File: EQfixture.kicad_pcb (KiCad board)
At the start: 2 copper layers, 149.8 x 111.4 mm, 14 parts, among them J1 Screw_Terminal_01x02, J2 Screw_Terminal_01x02, J3 Screw_Terminal_01x02, J4 Conn_02x10_Top_Bottom, J5 Screw_Terminal_01x03, J6 Conn_01x03, J7 Conn_01x06_Female

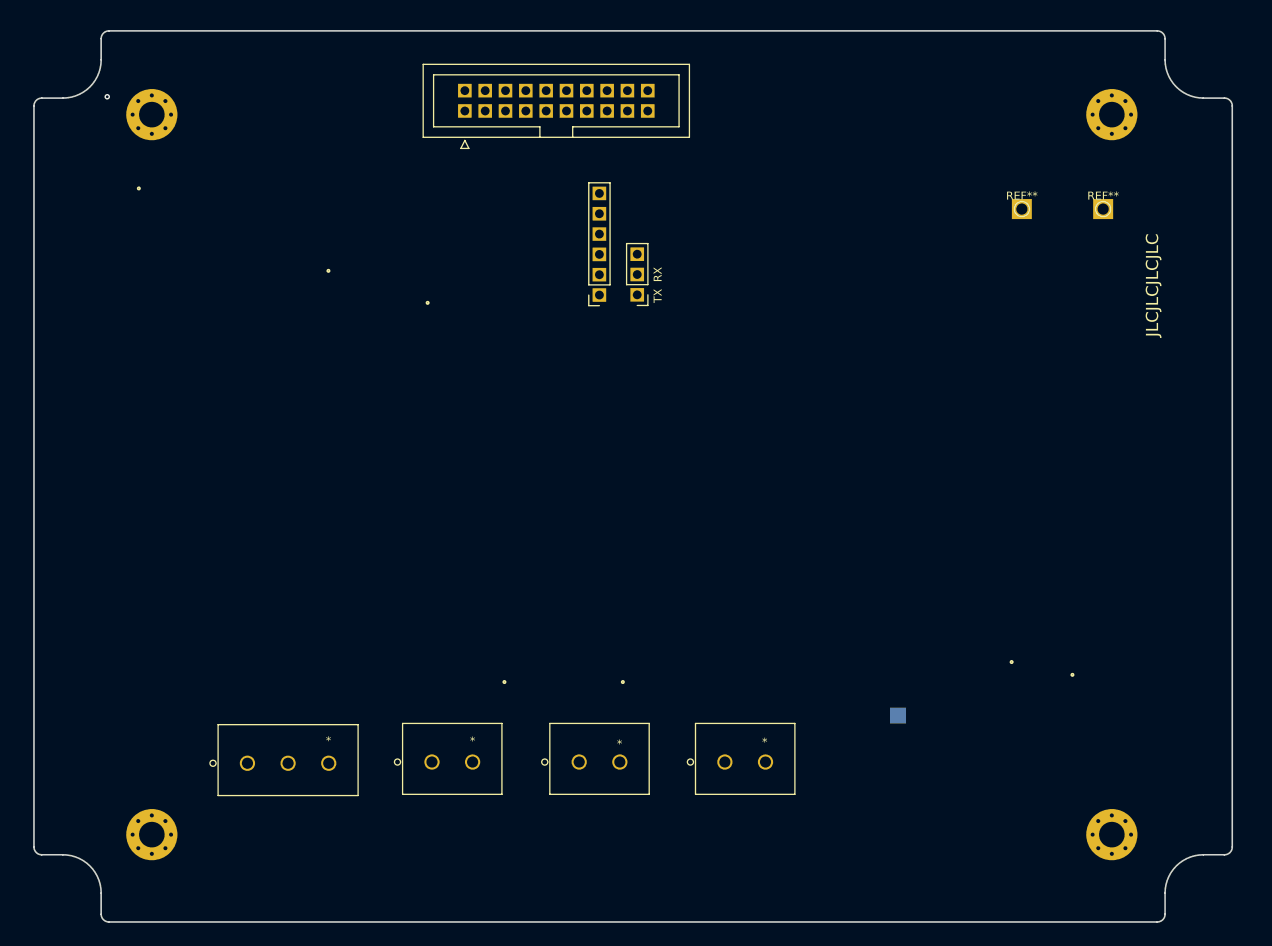
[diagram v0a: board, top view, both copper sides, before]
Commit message: pogos added
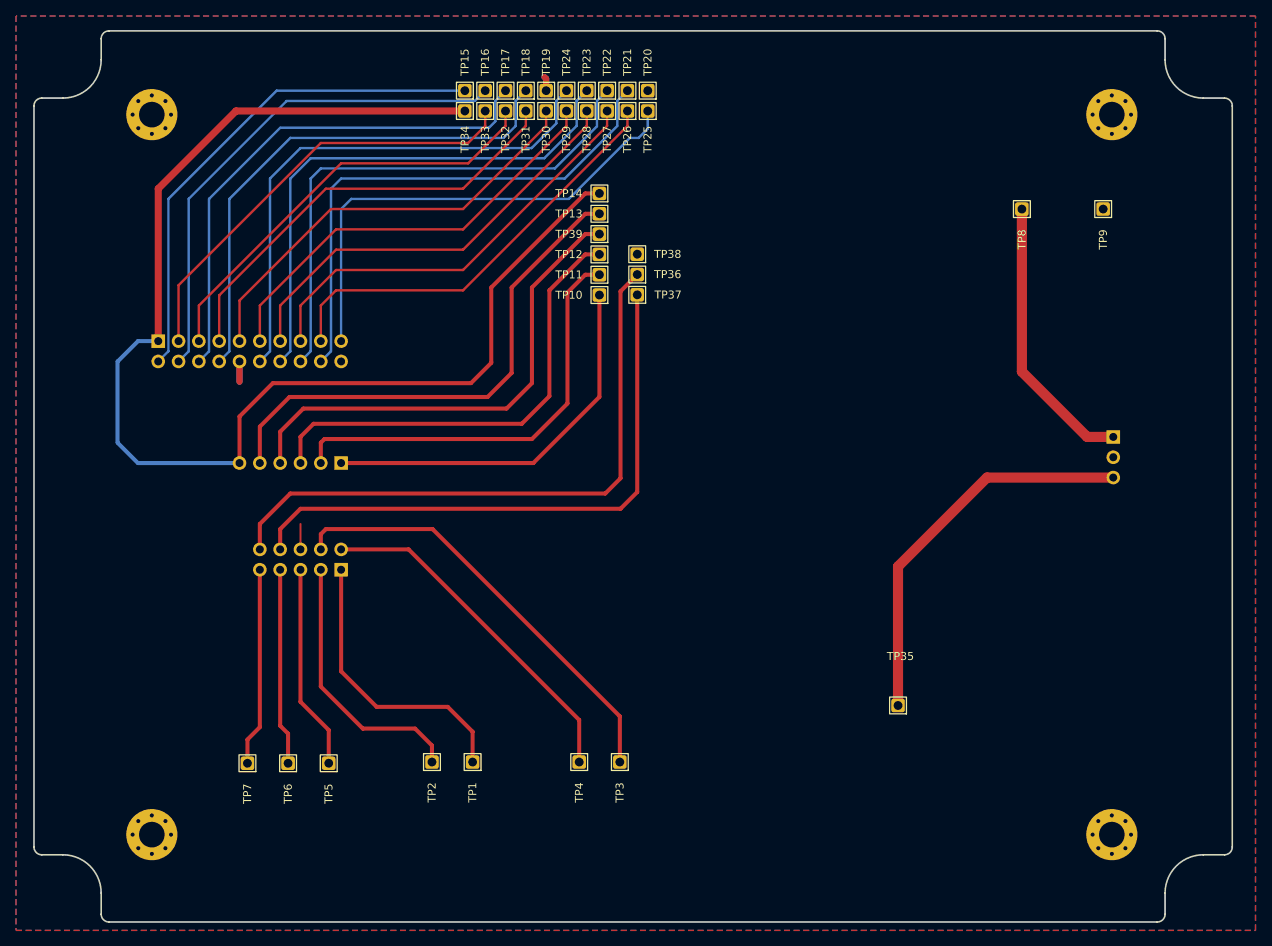
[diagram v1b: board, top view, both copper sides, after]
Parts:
- removed J5: Screw_Terminal_01x03, NLC:Phoenix_3P_1755749
- removed J6: Conn_01x03, Connector_PinHeader_2.54mm:PinHeader_1x03_P2.54mm_Vertical
- removed J7: Conn_01x06_Female, Connector_PinSocket_2.54mm:PinSocket_1x06_P2.54mm_Vertical
- removed REF** (x2): TestPoint_THTPad_D1.5mm_Drill0.7mm, TestPoint:TestPoint_THTPad_D1.5mm_Drill0.7mm
- added TP10: SWO, my_footprints:TestPoint-TH-Square-1mmHole, F.Cu at (145.5, 67.6)
- added TP11: NRST, my_footprints:TestPoint-TH-Square-1mmHole, F.Cu at (145.5, 65.1)
- added TP12: GND, my_footprints:TestPoint-TH-Square-1mmHole, F.Cu at (145.5, 62.5)
- added TP13: SWCLK, my_footprints:TestPoint-TH-Square-1mmHole, F.Cu at (145.5, 57.4)
- added TP14: 3V3, my_footprints:TestPoint-TH-Square-1mmHole, F.Cu at (145.5, 54.9)
- added TP15: I2C_SDA, my_footprints:TestPoint-TH-Square-1mmHole, F.Cu at (128.7, 42.1)
- added TP16: ~{LED_BAT_OK}, my_footprints:TestPoint-TH-Square-1mmHole, F.Cu at (131.2, 42.1)
- added TP17: ~{LED_FAIL}, my_footprints:TestPoint-TH-Square-1mmHole, F.Cu at (133.7, 42.1)
- added TP18: ~{LED_TRIGGER}, my_footprints:TestPoint-TH-Square-1mmHole, F.Cu at (136.3, 42.1)
- added TP19: GND, my_footprints:TestPoint-TH-Square-1mmHole, F.Cu at (138.8, 42.1)
- added TP2: R_TST_G, my_footprints:TestPoint-TH-Square-1mmHole, F.Cu at (124.5, 126.0)
- added TP20: GND, my_footprints:TestPoint-TH-Square-1mmHole, F.Cu at (151.5, 42.1)
- added TP21: LED_BAT_DONE, my_footprints:TestPoint-TH-Square-1mmHole, F.Cu at (149.0, 42.1)
- added TP22: SW_UP, my_footprints:TestPoint-TH-Square-1mmHole, F.Cu at (146.4, 42.1)
- added TP23: SW_TST_EVENT, my_footprints:TestPoint-TH-Square-1mmHole, F.Cu at (143.9, 42.1)
- added TP24: SW_RST_EVENT, my_footprints:TestPoint-TH-Square-1mmHole, F.Cu at (141.4, 42.1)
- added TP25: LED_BAT_CHRG, my_footprints:TestPoint-TH-Square-1mmHole, F.Cu at (151.5, 44.6)
- added TP26: SW_DOWN, my_footprints:TestPoint-TH-Square-1mmHole, F.Cu at (149.0, 44.6)
- added TP27: SW_ENTER, my_footprints:TestPoint-TH-Square-1mmHole, F.Cu at (146.4, 44.6)
- added TP28: SW_EXIT, my_footprints:TestPoint-TH-Square-1mmHole, F.Cu at (143.9, 44.6)
- added TP29: LED_RUNNING, my_footprints:TestPoint-TH-Square-1mmHole, F.Cu at (141.4, 44.6)
- added TP3: R_RST, my_footprints:TestPoint-TH-Square-1mmHole, F.Cu at (148.0, 126.0)
- added TP30: LED_TRIGGER, my_footprints:TestPoint-TH-Square-1mmHole, F.Cu at (138.8, 44.6)
- added TP31: LED_FAIL, my_footprints:TestPoint-TH-Square-1mmHole, F.Cu at (136.3, 44.6)
- added TP32: LED_STANDBY, my_footprints:TestPoint-TH-Square-1mmHole, F.Cu at (133.7, 44.6)
- added TP33: I2C_SCL, my_footprints:TestPoint-TH-Square-1mmHole, F.Cu at (131.2, 44.6)
- added TP34: 3V3, my_footprints:TestPoint-TH-Square-1mmHole, F.Cu at (128.7, 44.6)
- added TP35: VCC_BATT, my_footprints:TestPoint-TH-Square-1mmHole, F.Cu at (182.8, 118.9)
- added TP36: RX, my_footprints:TestPoint-TH-Square-1mmHole, F.Cu at (150.2, 65.0)
- added TP37: TX, my_footprints:TestPoint-TH-Square-1mmHole, F.Cu at (150.2, 67.6)
- added TP38: GND, my_footprints:TestPoint-TH-Square-1mmHole, F.Cu at (150.2, 62.5)
- added TP39: SWDIO, my_footprints:TestPoint-TH-Square-1mmHole, F.Cu at (145.5, 60.0)
- added TP4: R_RST_G, my_footprints:TestPoint-TH-Square-1mmHole, F.Cu at (143.0, 126.0)
- added TP5: R_NC, my_footprints:TestPoint-TH-Square-1mmHole, F.Cu at (111.6, 126.1)
- added TP6: R_COM, my_footprints:TestPoint-TH-Square-1mmHole, F.Cu at (106.6, 126.1)
- added TP7: R_NA, my_footprints:TestPoint-TH-Square-1mmHole, F.Cu at (101.5, 126.1)
- added TP8: 5VCC, my_footprints:TestPoint-TH-Square-1mmHole, F.Cu at (198.3, 56.9)
- added TP9: GND, my_footprints:TestPoint-TH-Square-1mmHole, F.Cu at (208.4, 56.9)
- J1: value Screw_Terminal_01x02 -> Conn_02x10_Top_Bottom; footprint NLC:Phoenix_2P_1755736 -> Connector_PinHeader_2.54mm:PinHeader_2x10_P2.54mm_Vertical; moved to B.Cu
- J2: value Screw_Terminal_01x02 -> Conn_02x05_Top_Bottom; footprint NLC:Phoenix_2P_1755736 -> Connector_PinHeader_2.54mm:PinHeader_2x05_P2.54mm_Vertical; moved to B.Cu
- J3: value Screw_Terminal_01x02 -> Conn_01x06; footprint NLC:Phoenix_2P_1755736 -> Connector_PinHeader_2.54mm:PinHeader_1x06_P2.54mm_Vertical; moved to B.Cu
- J4: value Conn_02x10_Top_Bottom -> Conn_01x03; footprint Connector_IDC:IDC-Header_2x10_P2.54mm_Vertical -> Connector_PinHeader_2.54mm:PinHeader_1x03_P2.54mm_Vertical; moved to B.Cu
- TP1: value VCC_TP -> R_TST; footprint TestPoint:TestPoint_Pad_2.0x2.0mm -> my_footprints:TestPoint-TH-Square-1mmHole; moved to F.Cu
- moved J1 92.4 mm to (90.3, 72.1), turned to -90 degrees
- moved J4 90.7 mm to (209.7, 84.1), turned to 180 degrees
- moved TP1 53.6 mm to (129.6, 126.0), turned to 0 degrees
- moved J3 51.1 mm to (113.2, 87.3), turned to 90 degrees
- moved J2 29.1 mm to (113.2, 100.7), turned to 90 degrees
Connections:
- H1 pad 1: (no net) -> unconnected-(H1-Pad1)
- H2 pad 1: (no net) -> unconnected-(H2-Pad1)
- H3 pad 1: (no net) -> unconnected-(H3-Pad1)
- H4 pad 1: (no net) -> unconnected-(H4-Pad1)
- J1 pad 1: (no net) -> +3V3
- J1 pad 2: (no net) -> /I2C1_SDA
- J2 pad 1: (no net) -> Net-(J2-Pin_1)
- J2 pad 2: (no net) -> Net-(J2-Pin_2)
- J3 pad 1: (no net) -> Net-(J3-Pin_1)
- J3 pad 2: (no net) -> Net-(J3-Pin_2)
- J4 pad 1: (no net) -> Net-(J4-Pin_1)
- J4 pad 2: (no net) -> GND
- J4 pad 3: (no net) -> Net-(J4-Pin_3)
- TP1 pad 1: (no net) -> Net-(J2-Pin_1)
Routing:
- net +3V3: track 0.00 -> 161.9 mm
- net Net-(J2-Pin_10): track 0.00 -> 76.9 mm
- net Net-(J2-Pin_8): track 0.00 -> 73.7 mm
- net GND: track 0.00 -> 70.0 mm
- net /SW_UP: track 0.00 -> 66.9 mm
- net /SW_TST_EVENT: track 0.00 -> 66.8 mm
- net /SW_RST_EVENT: track 0.00 -> 66.6 mm
- net /LED_BAT_DONE: track 0.00 -> 66.1 mm
- net /~{LED_TRIGGER}: track 0.00 -> 65.3 mm
- net /~{LED_FAIL}: track 0.00 -> 65.0 mm
- net Net-(J3-Pin_5): track 0.00 -> 64.3 mm
- net /~{LED_BAT_OK}: track 0.00 -> 63.5 mm
- net /I2C1_SDA: track 0.00 -> 63.5 mm
- net /LED_BAT_CHRG: track 0.00 -> 61.2 mm
- net Net-(J3-Pin_4): track 0.00 -> 61.1 mm
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- added copper zone on B.Cu, net GND
- added copper zone on F.Cu, net GND
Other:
- board text removed: "RX"
- board text removed: "TX"

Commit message: done + gerber added
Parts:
- H1, H2, H3, H4: footprint MountingHole:MountingHole_3.2mm_M3_Pad_Via -> MountingHole:MountingHole_3.2mm_M3_Pad
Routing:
- net GND: track 70.0 -> 73.8 mm
- net /LED_STANDBY: track 53.9 -> 55.4 mm
- net Net-(J2-Pin_10): track 76.9 -> 77.7 mm
- net /I2C1_SCL: track 55.4 -> 56.1 mm
- net /LED_BAT_CHRG: track 61.2 -> 60.6 mm
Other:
- board text added: "EQRELE V1.7 Test Jig"
